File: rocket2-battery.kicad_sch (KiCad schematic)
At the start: 83 parts, among them J2 Conn_01x07, J4 SMA, J5 ARM Cortex Debug, P5 PAD_SMD, P6 PAD_SMD, Q2 Q_NMOS_GSD, Q3 Q_NMOS_GSD, Q4 PMOS, Q5 PMOS, Q6 Q_NMOS_GSD, Q7 Q_NMOS_GSD, Q8 PMOS, Q9 PMOS, U5 ADS7828, U6 LM2596S-3.3, U7 LM2596S-5, Y1 16MHz

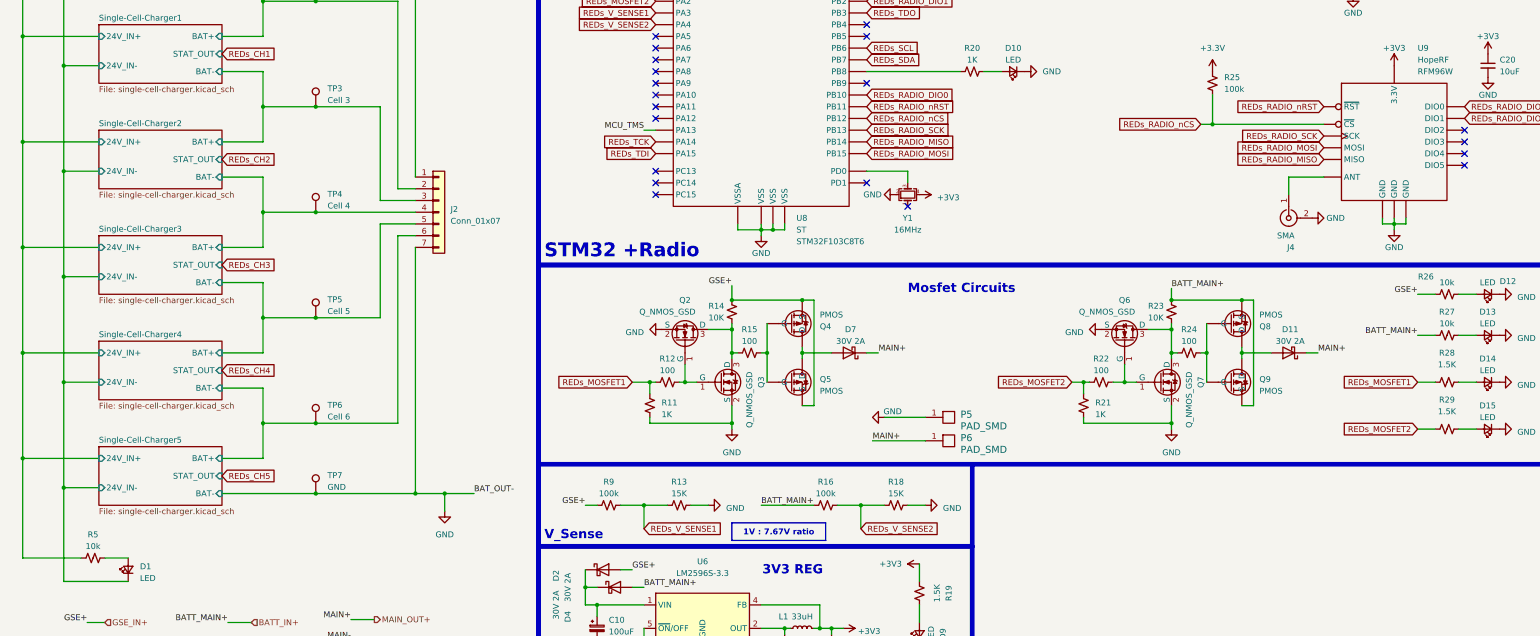
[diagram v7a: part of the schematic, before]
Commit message: Assigned almost all footprints
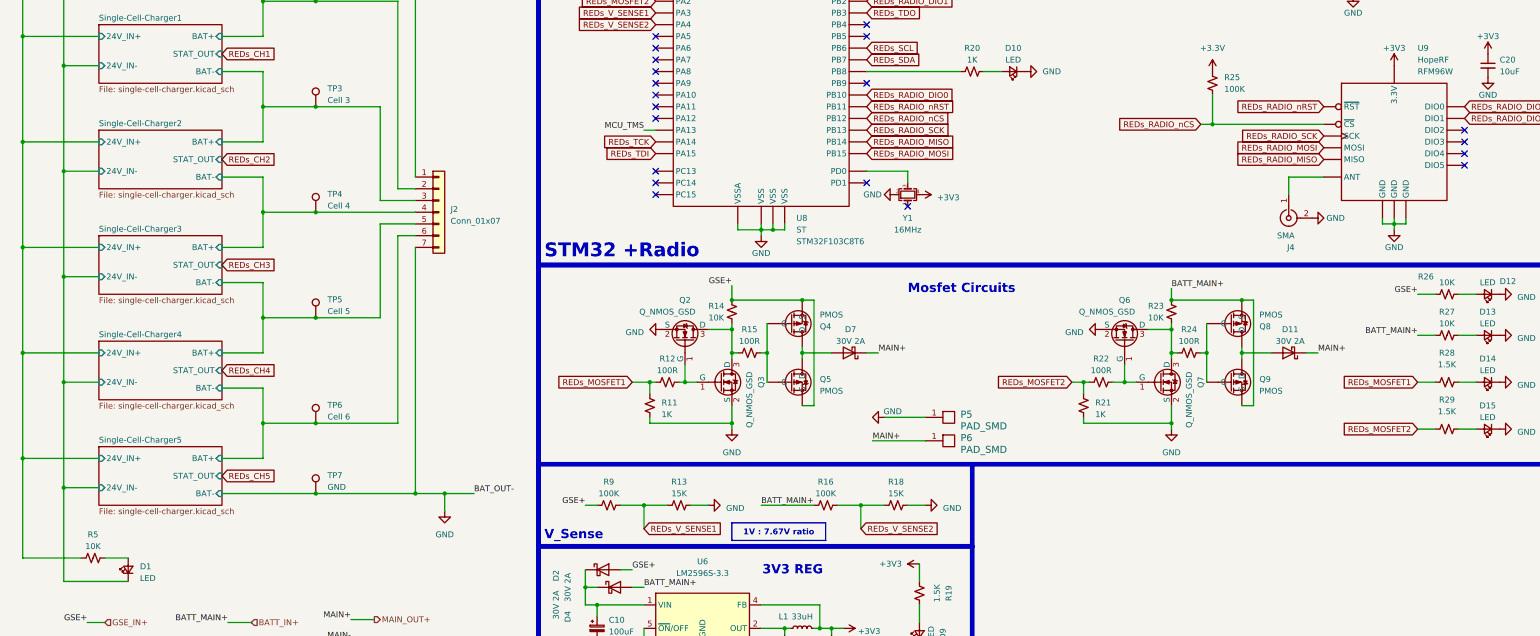
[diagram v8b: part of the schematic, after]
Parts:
- C10, C11: footprint (none) -> Capacitor_SMD:CP_Elec_10x10
- C14, C20: footprint Capacitor_SMD:C_0603_1608Metric_Pad1.08x0.95mm_HandSolder -> Capacitor_SMD:C_0603_1608Metric
- C15, C16, C17, C18, C19, C9: footprint Capacitor_SMD:C_0603_1608Metric_Pad1.08x0.95mm_HandSolder -> Capacitor_SMD:C_0402_1005Metric; Part # Generic 0603 100nF 6.3V X7R MLCC -> Generic 100nF 6.3V X7R 0402 MLCC
- C7: footprint (none) -> Capacitor_SMD:C_0603_1608Metric; Part # (none) -> Generic 0603 4.7uF 6.3V X7R MLCC
- C8: footprint (none) -> Capacitor_SMD:C_0603_1608Metric; Part # (none) -> Generic 0603 0.1uF 6.3V X7R MLCC
- D10: footprint Diode_SMD:D_0603_1608Metric_Pad1.05x0.95mm_HandSolder -> LED_SMD:LED_0603_1608Metric_Pad1.05x0.95mm_HandSolder
- D5, D6: footprint (none) -> Diode_SMD:D_SMC
- L1, L2: footprint (none) -> Inductor_SMD:L_12x12mm_H8mm
- R10, R14, R23: footprint Resistor_SMD:R_0603_1608Metric_Pad0.98x0.95mm_HandSolder -> Resistor_SMD:R_0402_1005Metric; Part # Generic 0603 10K 1% Resistor -> Generic 10K 1% 0402 Resistor
- R11, R21: footprint Resistor_SMD:R_0603_1608Metric_Pad0.98x0.95mm_HandSolder -> Resistor_SMD:R_0402_1005Metric; Part # Generic 0603 1K 10% Resistor -> Generic 1K 1% 0402 Resistor
- R12, R15, R22, R24: value 100 -> 100R; footprint Resistor_SMD:R_0603_1608Metric_Pad0.98x0.95mm_HandSolder -> Resistor_SMD:R_0402_1005Metric; Part # Generic 0603 100ohm 5% Resistor -> Generic 100R 1% 0402 Resistor
- R13, R18: footprint Resistor_SMD:R_0603_1608Metric_Pad0.98x0.95mm_HandSolder -> Resistor_SMD:R_0402_1005Metric; Part # Generic 0603 15K 0.1% Resistor -> Generic 0402 15K 0.1% Resistor
- R16, R9: value 100k -> 100K; footprint Resistor_SMD:R_0603_1608Metric_Pad0.98x0.95mm_HandSolder -> Resistor_SMD:R_0402_1005Metric; Part # Generic 0603 100K 0.1% Resistor -> Generic 100K 5% 0402 Resistor
- R17, R19, R28, R29: footprint Resistor_SMD:R_0603_1608Metric_Pad0.98x0.95mm_HandSolder -> Resistor_SMD:R_0402_1005Metric; Part # Generic 0603 10K 5% Resistor -> Generic 0402 1.5K 0.1% Resistor
- R20: footprint Resistor_SMD:R_0603_1608Metric_Pad0.98x0.95mm_HandSolder -> Resistor_SMD:R_0402_1005Metric; Part # Generic 0603 1K 1% Resistor -> Generic 1K 1% 0402 Resistor
- R25: value 100k -> 100K; footprint Resistor_SMD:R_0603_1608Metric_Pad0.98x0.95mm_HandSolder -> Resistor_SMD:R_0402_1005Metric; Part # Generic 100k 1% 0402 Chip Resistor -> Generic 100K 5% 0402 Resistor
- R26, R27, R5: value 10k -> 10K; footprint Resistor_SMD:R_0603_1608Metric_Pad0.98x0.95mm_HandSolder -> Resistor_SMD:R_0402_1005Metric; Part # Generic 0603 10K 5% Resistor -> Generic 10K 1% 0402 Resistor
- R6: footprint (none) -> Resistor_SMD:R_0402_1005Metric; Part # (none) -> Generic 5R 0402 Resistor
- R7, R8: footprint (none) -> Resistor_SMD:R_0402_1005Metric; Part # (none) -> Generic 2K 5% 0402 Resistor
- U9: footprint UCIRP-KiCAD-Lib:RFM95W -> 0UCIRP-KiCAD-Lib:RFM95W
